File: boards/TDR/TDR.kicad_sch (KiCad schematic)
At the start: 18 parts, among them J1 USB_C_Receptacle_USB2.0, J2 SMA, U10 W25Q128JVPIQ, U14 Resistive_Power_Divider, U2 USBLC6-2SC6, U3 AX3DBF1-200.0000

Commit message: change crystal footprint and roughly finish schematic
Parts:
- U3: value AX3DBF1-200.0000 -> AxxDBF1-200.0000; footprint Moje:Oscillator_SMD_Abracon_LGA-6_2.5x3.2mm_P1.2mm -> Oscillator:Oscillator_SMD_IDT_JS6-6_5.0x3.2mm_P1.27mm
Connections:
- net FPGA_Power/5V_INPUT renamed DAC/5V_INPUT
- net VCCHTX0 renamed +1V2_CORE
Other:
- sheet DAC ports: added 5V_INPUT, VCCA; removed none
- sheet FPGA_IO ports: added none; removed DAC0_BITSTREAM, DAC1_BITSTREAM, RX_D0CH1_N, RX_D0CH1_P, TX_D0CH1_N, TX_D0CH1_P
- sheet FPGA_Power ports: added VCCA, VCCHTX; removed none

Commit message: change usb footprint, route a few connections
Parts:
- J1: footprint Connector_USB:USB_C_Receptacle_GCT_USB4085 -> Moje:USB_C_Receptacle_JAE_DX07S016
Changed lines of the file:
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@@
-(kicad_sch (version 20200618) (host eeschema "(5.99.0-2073-gbb1afb747)")
+(kicad_sch (version 20200618) (host eeschema "(5.99.0-2195-g476558ece)")
   (page 1 5)
   (paper "A4")
@@
   (junction (at 227.33 116.84) (diameter 0) (color 0 0 0 0))
   (junction (at 236.22 128.27) (diameter 0) (color 0 0 0 0))
+  (no_connect (at 146.685 150.495))
+  (no_connect (at 53.975 88.9))
   (no_connect (at 53.975 91.44))
-  (no_connect (at 53.975 88.9))
-  (no_connect (at 146.685 150.495))
   (wire (pts (xy 31.115 99.06) (xy 31.115 100.33))
     (stroke (width 0) (type solid) (color 0 0 0 0))
@@
     (property "Reference" "J1" (id 0) (at 41.4528 54.2036 0))
     (property "Value" "USB_C_Receptacle_USB2.0" (id 1) (at 41.4528 56.515 0))
-    (property "Footprint" "Connector_USB:USB_C_Receptacle_GCT_USB4085" (id 2) (at 42.545 76.2 0)
-      (effects (font (size 1.27 1.27)) hide)
-    )
+    (property "Footprint" "Moje:USB_C_Receptacle_JAE_DX07S016" (id 2) (at 42.545 76.2 0)
+      (effects (font (size 1.27 1.27)) hide)
+    )

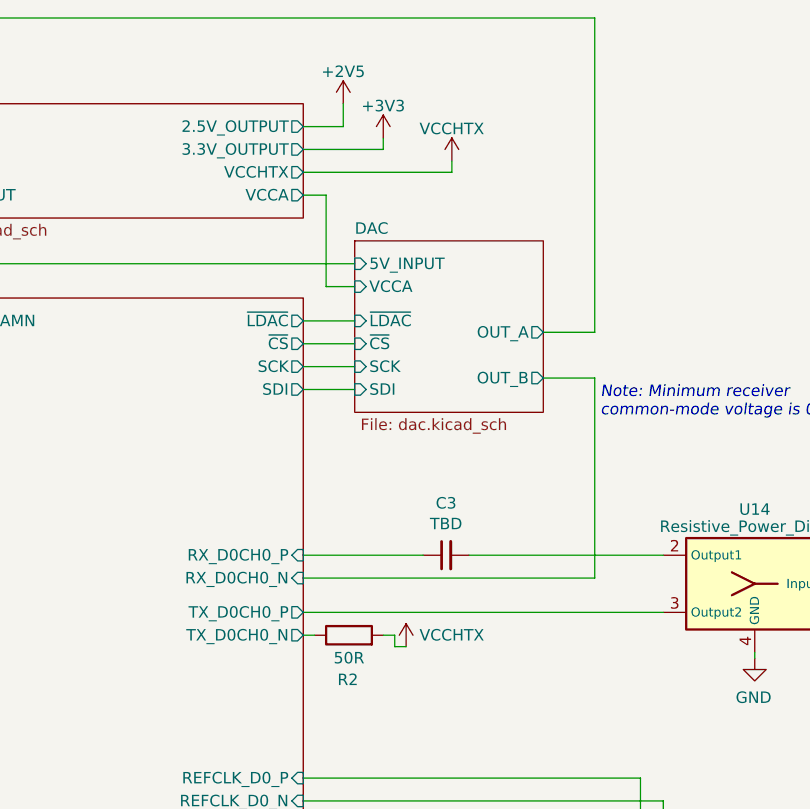
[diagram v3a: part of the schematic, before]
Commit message: route almost all nets except VCCA, VCCAUX and maybe some others
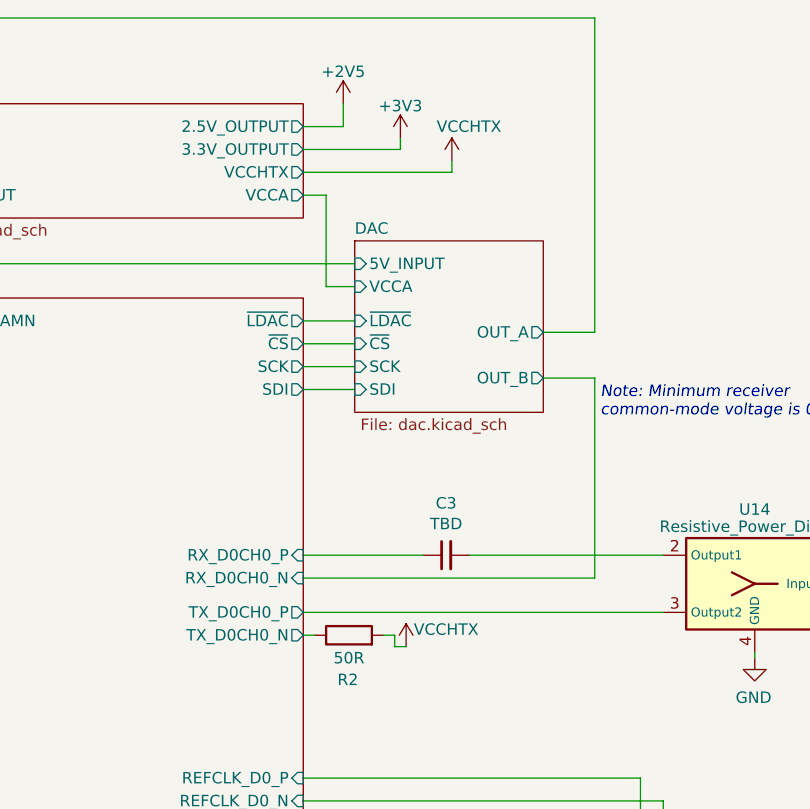
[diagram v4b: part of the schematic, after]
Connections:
- net +1V2_CORE renamed VCCHTX
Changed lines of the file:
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@@
-(kicad_sch (version 20200618) (host eeschema "(5.99.0-2195-g476558ece)")
+(kicad_sch (version 20200618) (host eeschema "(5.99.0-2241-g37ce9fb84)")
   (page 1 5)
   (paper "A4")
@@
   (junction (at 227.33 116.84) (diameter 0) (color 0 0 0 0))
   (junction (at 236.22 128.27) (diameter 0) (color 0 0 0 0))
+  (no_connect (at 53.975 91.44))
   (no_connect (at 53.975 88.9))
   (no_connect (at 146.685 150.495))
-  (no_connect (at 53.975 91.44))
   (wire (pts (xy 31.115 99.06) (xy 31.115 100.33))
     (stroke (width 0) (type solid) (color 0 0 0 0))
@@
     (stroke (width 0) (type solid) (color 0 0 0 0))
   )
-  (wire (pts (xy 208.28 34.29) (xy 217.17 34.29))
+  (wire (pts (xy 208.28 34.29) (xy 219.075 34.29))
     (stroke (width 0) (type solid) (color 0 0 0 0))
   )
@@
     (stroke (width 0) (type solid) (color 0 0 0 0))
   )
-  (wire (pts (xy 217.17 34.29) (xy 217.17 33.02))
-    (stroke (width 0) (type solid) (color 0 0 0 0))
-  )
   (wire (pts (xy 217.17 88.265) (xy 218.44 88.265))
     (stroke (width 0) (type solid) (color 0 0 0 0))
@@
   )
   (wire (pts (xy 218.44 89.535) (xy 219.71 89.535))
+    (stroke (width 0) (type solid) (color 0 0 0 0))
+  )
+  (wire (pts (xy 219.075 34.29) (xy 219.075 33.02))
     (stroke (width 0) (type solid) (color 0 0 0 0))
   )
@@
     )
   )
-  (symbol (lib_id "power:+3V3") (at 217.17 33.02 0) (unit 1)
-    (in_bom yes) (on_board yes)
-    (property "Reference" "#PWR0162" (id 0) (at 217.17 36.83 0)
-      (effects (font (size 1.27 1.27)) hide)
-    )
-    (property "Value" "+3V3" (id 1) (at 217.17 29.464 0))
-    (property "Footprint" "" (id 2) (at 217.17 33.02 0)
-      (effects (font (size 1.27 1.27)) hide)
-    )
-    (property "Datasheet" "" (id 3) (at 217.17 33.02 0)
-      (effects (font (size 1.27 1.27)) hide)
-    )
-  )
   (symbol (lib_id "power:+2V5") (at 217.17 115.57 0) (unit 1)
     (in_bom yes) (on_board yes)
@@
     )
   )
+  (symbol (lib_id "power:+3V3") (at 219.075 33.02 0) (unit 1)
+    (in_bom yes) (on_board yes)
+    (property "Reference" "#PWR0162" (id 0) (at 219.075 36.83 0)
+      (effects (font (size 1.27 1.27)) hide)
+    )
+    (property "Value" "+3V3" (id 1) (at 219.075 29.464 0))
+    (property "Footprint" "" (id 2) (at 219.075 33.02 0)
+      (effects (font (size 1.27 1.27)) hide)
+    )
+    (property "Datasheet" "" (id 3) (at 219.075 33.02 0)
+      (effects (font (size 1.27 1.27)) hide)
+    )
+  )
   (symbol (lib_id "Moje:VCCHTX") (at 219.71 89.535 0) (unit 1)
     (in_bom yes) (on_board yes)
-    (property "Reference" "#PWR0141" (id 0) (at 219.71 93.345 0)
-      (effects (font (size 1.27 1.27)) hide)
-    )
-    (property "Value" "VCCHTX" (id 1) (at 224.79 88.265 0))
+    (property "Reference" "#PWR0140" (id 0) (at 219.71 93.345 0)
+      (effects (font (size 1.27 1.27)) hide)
+    )
+    (property "Value" "VCCHTX" (id 1) (at 224.155 87.63 0))
     (property "Footprint" "" (id 2) (at 219.71 89.535 0)
       (effects (font (size 1.27 1.27)) hide)
@@
     )
   )
-  (symbol (lib_id "Moje:VCCHTX") (at 224.79 35.56 0) (unit 1)
-    (in_bom yes) (on_board yes)
-    (property "Reference" "#PWR0140" (id 0) (at 224.79 39.37 0)
-      (effects (font (size 1.27 1.27)) hide)
-    )
-    (property "Value" "VCCHTX" (id 1) (at 224.79 32.004 0))
+  (symbol (lib_name "Moje:VCCHTX_1") (lib_id "Moje:VCCHTX") (at 224.79 35.56 0) (unit 1)
+    (in_bom yes) (on_board yes)
+    (property "Reference" "#PWR?" (id 0) (at 224.79 39.37 0)
+      (effects (font (size 1.27 1.27)) hide)
+    )
+    (property "Value" "VCCHTX" (id 1) (at 226.695 31.75 0))
     (property "Footprint" "" (id 2) (at 224.79 35.56 0)
       (effects (font (size 1.27 1.27)) hide)
@@
       (reference "#PWR0117") (unit 1)
     )
-    (path "/cb0ba945-1be9-4ca5-9324-38f58a42b78d"
+    (path "/abf43df2-1fe3-4ff3-aa2c-b089ee30d8f5"
       (reference "#PWR0140") (unit 1)
-    )
-    (path "/82dd3d05-9fc7-4715-96fe-d76685437adb"
-      (reference "#PWR0141") (unit 1)
     )
     (path "/00000000-0000-0000-0000-00005e90d967"
@@
       (reference "#PWR0188") (unit 1)
     )
+    (path "/9e62276d-c158-4841-b11b-e15bca5f9b5f"
+      (reference "#PWR?") (unit 1)
+    )
     (path "/00000000-0000-0000-0000-00005e721021"
       (reference "C2") (unit 1)
@@
       (reference "#PWR012") (unit 1)
     )
+    (path "/f9fc04fe-099d-4539-8ef8-fc25a0dbd2d1/4afe8f3b-9c22-4549-99f6-83cde47516df"
+      (reference "#PWR0145") (unit 1)
+    )
     (path "/f9fc04fe-099d-4539-8ef8-fc25a0dbd2d1/2728dc0a-4bfe-4587-8c7b-620684dd76c0"
       (reference "#PWR0186") (unit 1)
@@
       (reference "C4") (unit 1)
     )
+    (path "/f9fc04fe-099d-4539-8ef8-fc25a0dbd2d1/5be37440-54ab-4009-8376-244e24c26e87"
+      (reference "C23") (unit 1)
+    )
     (path "/f9fc04fe-099d-4539-8ef8-fc25a0dbd2d1/00000000-0000-0000-0000-00005ea176fb"

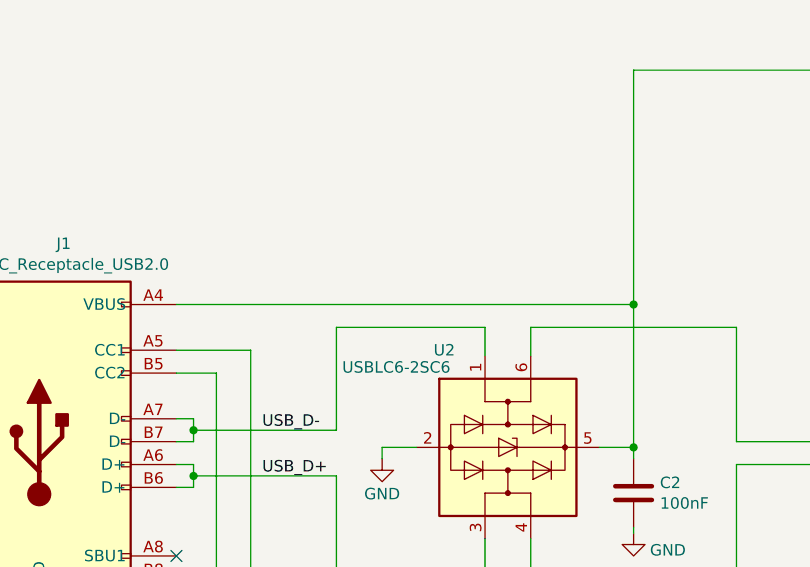
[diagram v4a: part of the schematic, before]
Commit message: solved DRC errors and routed few more nets
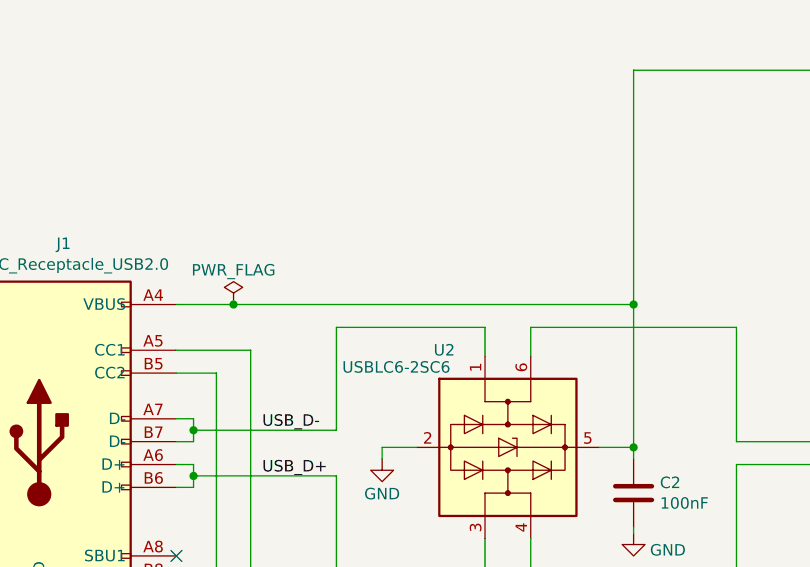
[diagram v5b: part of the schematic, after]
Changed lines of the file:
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@@
-(kicad_sch (version 20200618) (host eeschema "(5.99.0-2241-g37ce9fb84)")
+(kicad_sch (version 20200618) (host eeschema "(5.99.0-2250-gafd432e68)")
   (page 1 5)
   (paper "A4")
@@
   (junction (at 55.88 74.93) (diameter 0) (color 0 0 0 0))
   (junction (at 55.88 80.01) (diameter 0) (color 0 0 0 0))
+  (junction (at 60.325 60.96) (diameter 0) (color 0 0 0 0))
   (junction (at 104.775 60.96) (diameter 0) (color 0 0 0 0))
   (junction (at 104.775 76.835) (diameter 0) (color 0 0 0 0))
@@
   (junction (at 236.22 128.27) (diameter 0) (color 0 0 0 0))
   (no_connect (at 53.975 91.44))
+  (no_connect (at 146.685 150.495))
   (no_connect (at 53.975 88.9))
-  (no_connect (at 146.685 150.495))
   (wire (pts (xy 31.115 99.06) (xy 31.115 100.33))
     (stroke (width 0) (type solid) (color 0 0 0 0))
@@
     (stroke (width 0) (type solid) (color 0 0 0 0))
   )
-  (wire (pts (xy 53.975 60.96) (xy 104.775 60.96))
+  (wire (pts (xy 53.975 60.96) (xy 60.325 60.96))
     (stroke (width 0) (type solid) (color 0 0 0 0))
   )
@@
   )
   (wire (pts (xy 58.42 104.14) (xy 58.42 105.41))
+    (stroke (width 0) (type solid) (color 0 0 0 0))
+  )
+  (wire (pts (xy 60.325 60.96) (xy 104.775 60.96))
     (stroke (width 0) (type solid) (color 0 0 0 0))
   )
@@
     (effects (font (size 1.27 1.27)) (justify left bottom))
   )
+  (symbol (lib_id "power:PWR_FLAG") (at 60.325 60.96 0) (unit 1)
+    (in_bom yes) (on_board yes)
+    (property "Reference" "#FLG0101" (id 0) (at 60.325 59.055 0)
+      (effects (font (size 1.27 1.27)) hide)
+    )
+    (property "Value" "PWR_FLAG" (id 1) (at 60.325 57.15 0))
+    (property "Footprint" "" (id 2) (at 60.325 60.96 0)
+      (effects (font (size 1.27 1.27)) hide)
+    )
+    (property "Datasheet" "~" (id 3) (at 60.325 60.96 0)
+      (effects (font (size 1.27 1.27)) hide)
+    )
+  )
   (symbol (lib_id "power:+3V3") (at 136.525 117.475 0) (unit 1)
     (in_bom yes) (on_board yes)
@@
   (symbol (lib_name "Moje:VCCHTX_1") (lib_id "Moje:VCCHTX") (at 224.79 35.56 0) (unit 1)
     (in_bom yes) (on_board yes)
-    (property "Reference" "#PWR?" (id 0) (at 224.79 39.37 0)
+    (property "Reference" "#PWR0141" (id 0) (at 224.79 39.37 0)
       (effects (font (size 1.27 1.27)) hide)
     )
@@
   )
   (symbol_instances
+    (path "/f94e32c4-8186-443d-9e24-94914fac3496"
+      (reference "#FLG0101") (unit 1)
+    )
     (path "/00000000-0000-0000-0000-00005e720fa9"
       (reference "#PWR03") (unit 1)
@@
       (reference "#PWR0140") (unit 1)
     )
+    (path "/9e62276d-c158-4841-b11b-e15bca5f9b5f"
+      (reference "#PWR0141") (unit 1)
+    )
     (path "/00000000-0000-0000-0000-00005e90d967"
       (reference "#PWR0162") (unit 1)
@@
       (reference "#PWR0188") (unit 1)
     )
-    (path "/9e62276d-c158-4841-b11b-e15bca5f9b5f"
-      (reference "#PWR?") (unit 1)
-    )
     (path "/00000000-0000-0000-0000-00005e721021"
       (reference "C2") (unit 1)
@@
       (reference "#PWR0144") (unit 1)
     )
+    (path "/00000000-0000-0000-0000-00005e56b656/136f9f81-12e4-4b5b-b8e2-af1a090936d2"
+      (reference "#PWR0146") (unit 1)
+    )
     (path "/00000000-0000-0000-0000-00005e56b656/00000000-0000-0000-0000-00005e9277f1"
